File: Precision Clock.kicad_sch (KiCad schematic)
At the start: 0 parts

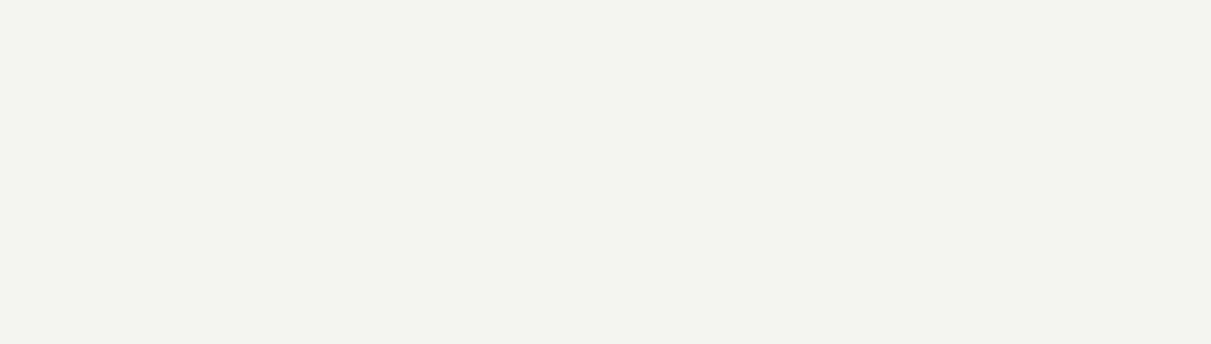
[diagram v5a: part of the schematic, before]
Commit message: ESD, LEDs, footprints
- assignment of footprints
- ESD protection
- User buttons
- addition of test points
- BOM consolidation of  resistors
- general reordering of the schematic
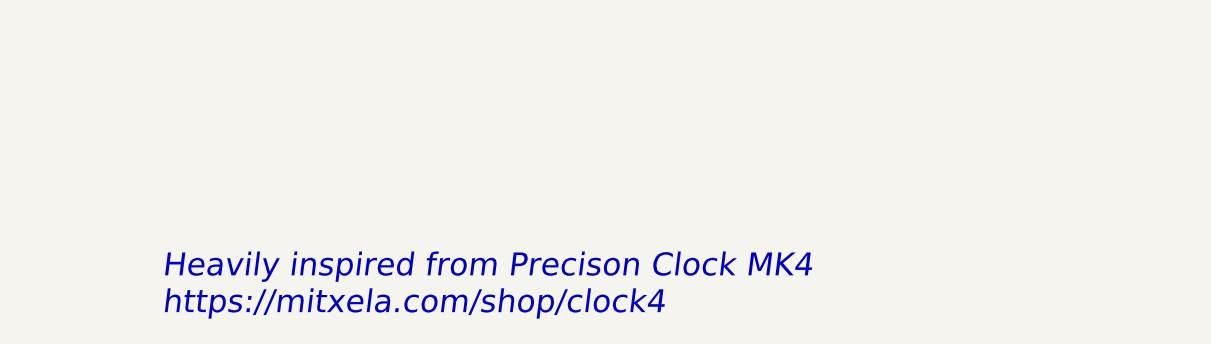
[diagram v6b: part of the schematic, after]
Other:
- note added: "Heavily inspired from Precison Clock MK4 https://mitxela.com/shop/clock4"
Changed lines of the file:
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@@
 	(title_block
 		(title "Precision Clock")
-		(date "2025-10-31")
+		(date "2025-11-04")
 		(rev "v0.0")
 		(company "Rajath Katker")
 		(comment 4 "Final verification pending")
 	)
+	(text "Heavily inspired from Precison Clock MK4\nhttps://mitxela.com/shop/clock4"
+		(exclude_from_sim no)
+		(at 84.836 184.404 0)
+		(effects
+			(font
+				(size 2.54 2.54)
+				(italic yes)
+				(color 194 0 0 1)
+			)
+			(justify left)
+		)
+	)
 	(bus

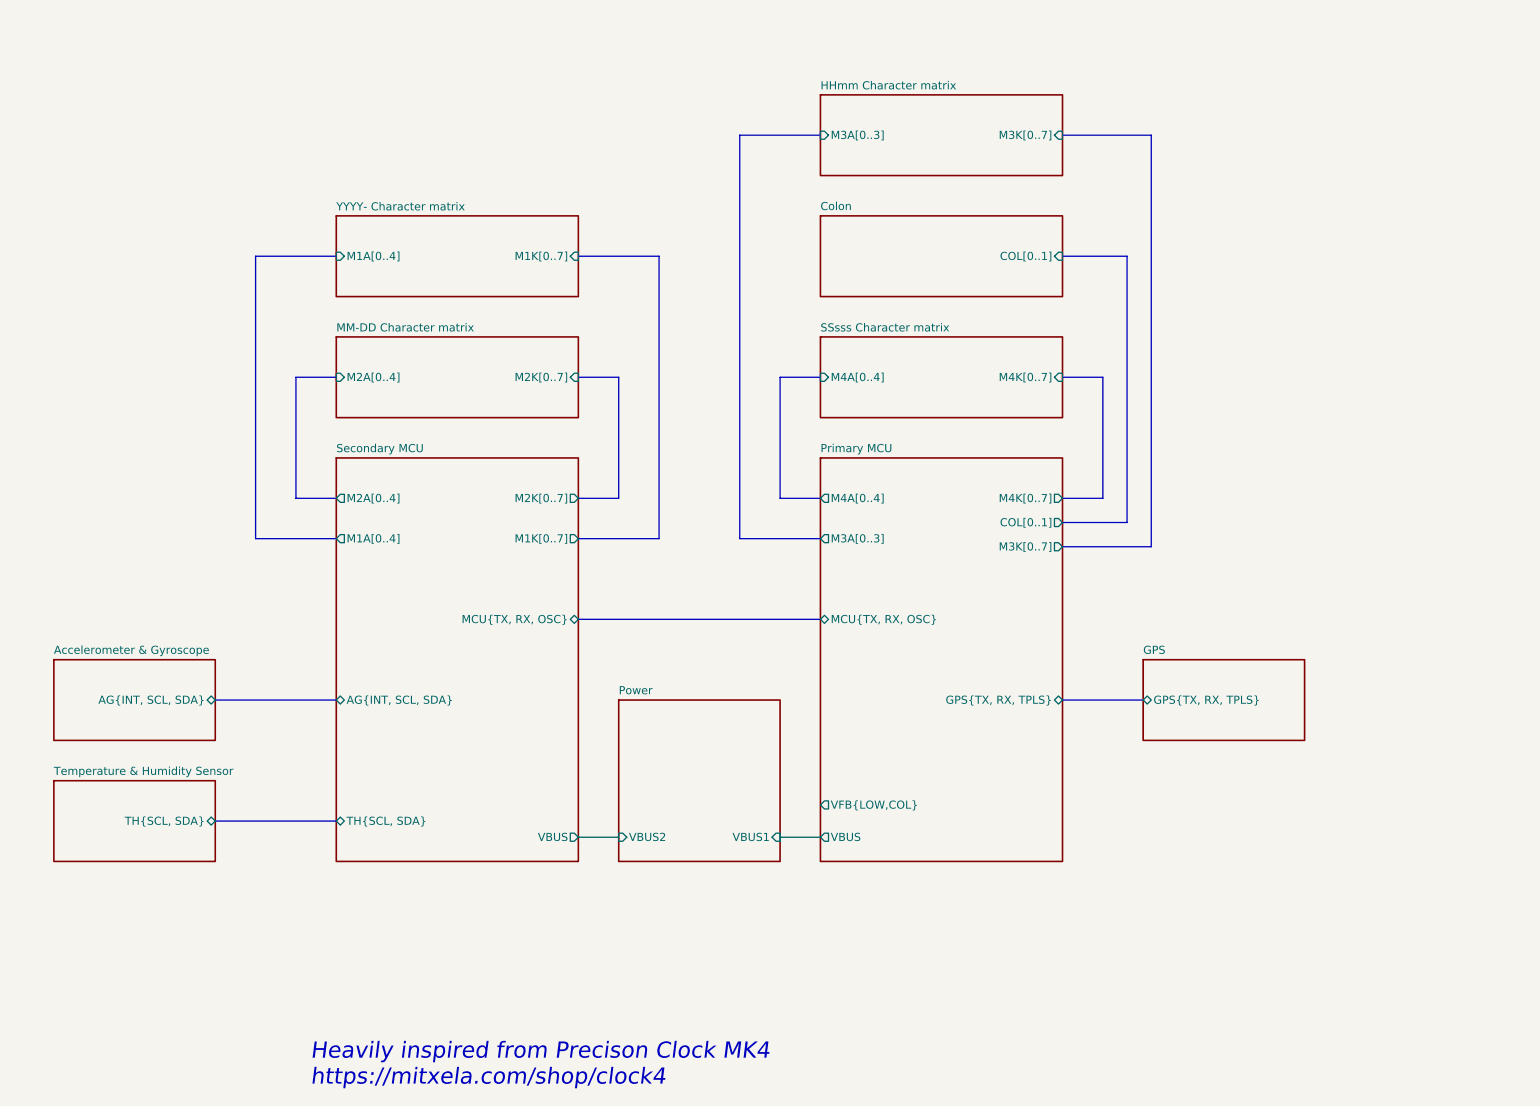
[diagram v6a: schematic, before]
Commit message: verification
- sensor schematic verification
- change in the value of current limiting resistor
- disconnected unused buffer pins
- labeling or peripherals used in primary MCU
- additional user button
- DRC corrections
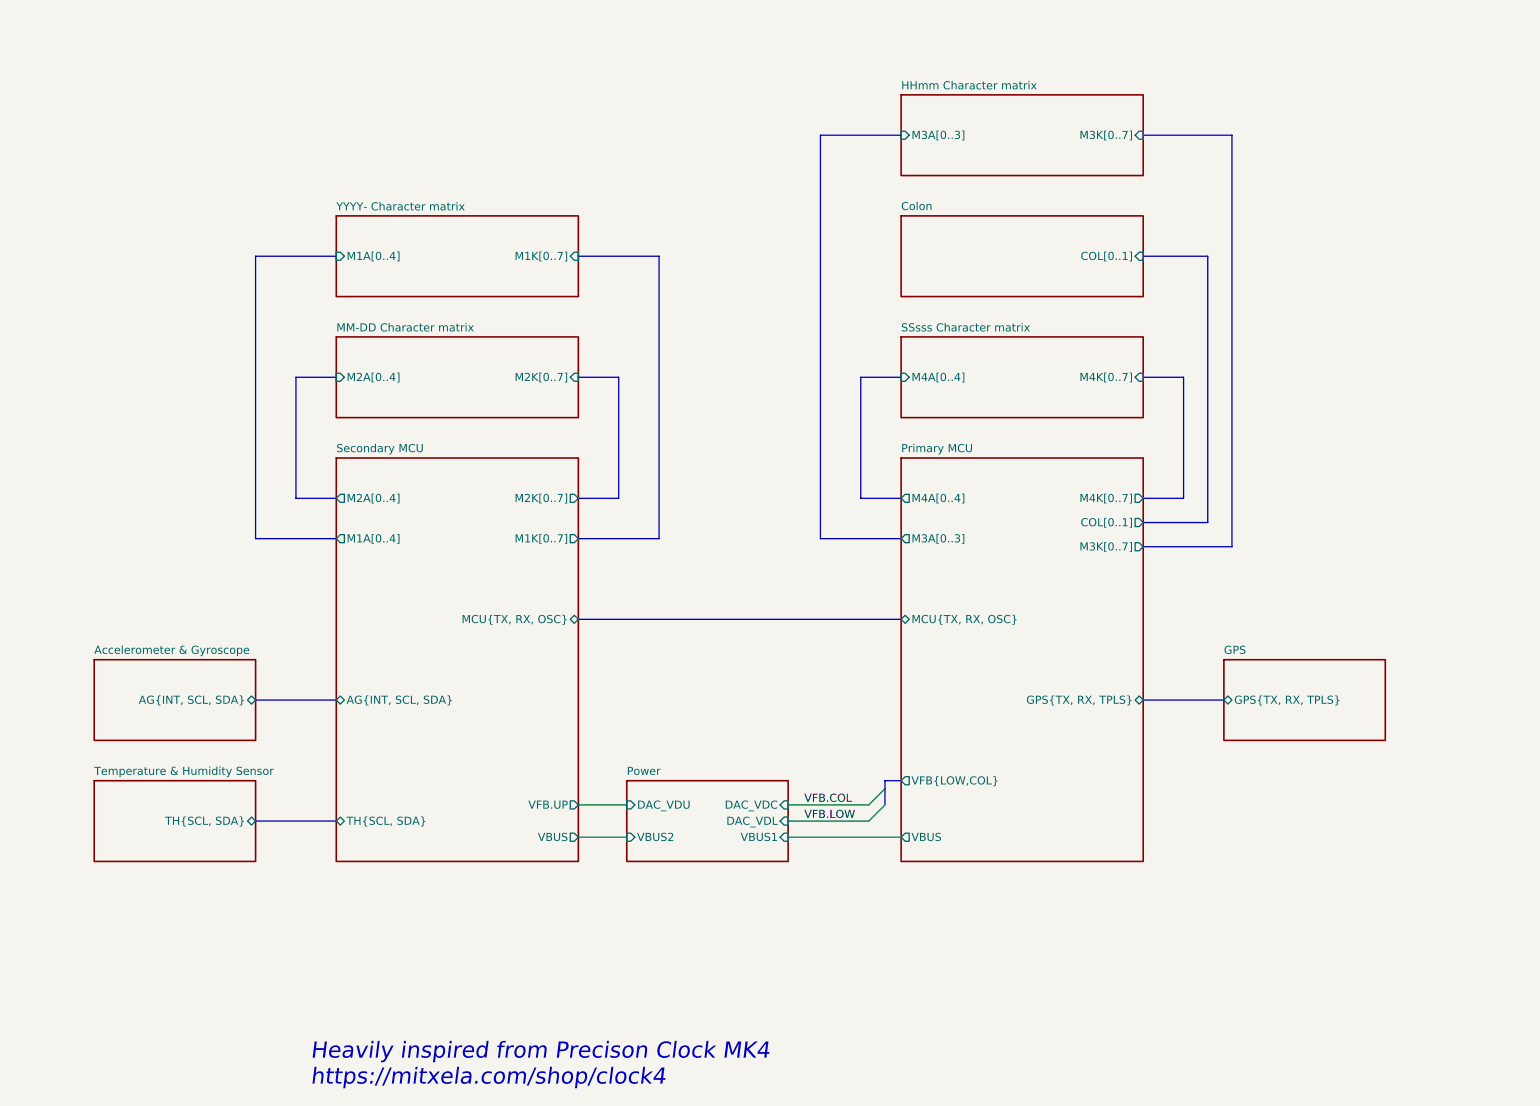
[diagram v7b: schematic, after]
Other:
- sheet Power ports: added DAC_VDC, DAC_VDL, DAC_VDU; removed none
- sheet Secondary MCU ports: added VFB.UP; removed none
- company: Rajath Katker -> TJ71PL
- title: Precision Clock -> Precision Clock　

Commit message: semi final verification
- change in display type to common cathode
- verification of the schematic
- addition of footprints
- further minor changes
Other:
- sheet HHmm Character matrix ports: added M3A[0..7], M3K[0..3]; removed M3A[0..3], M3K[0..7]
- sheet MM-DD Character matrix ports: added M2A[0..7], M2K[0..4]; removed M2A[0..4], M2K[0..7]
- sheet Primary MCU ports: added M3A[0..7], M3K[0..3], M4A[0..7], M4K[0..4]; removed M3A[0..3], M3K[0..7], M4A[0..4], M4K[0..7]
- sheet SSsss Character matrix ports: added M4A[0..7], M4K[0..4]; removed M4A[0..4], M4K[0..7]
- sheet Secondary MCU ports: added M1A[0..7], M1K[0..4], M2A[0..7], M2K[0..4]; removed M1A[0..4], M1K[0..7], M2A[0..4], M2K[0..7]
- sheet YYYY- Character matrix ports: added M1A[0..7], M1K[0..4]; removed M1A[0..4], M1K[0..7]
